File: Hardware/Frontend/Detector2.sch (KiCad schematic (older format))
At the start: 27 parts, among them J4 Conn_Coaxial, U4 OPA145ID, U5 OPA145ID, U6 OPA145ID

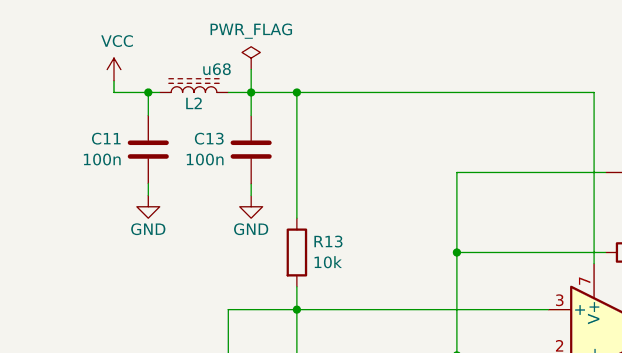
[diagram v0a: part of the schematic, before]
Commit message: add bom
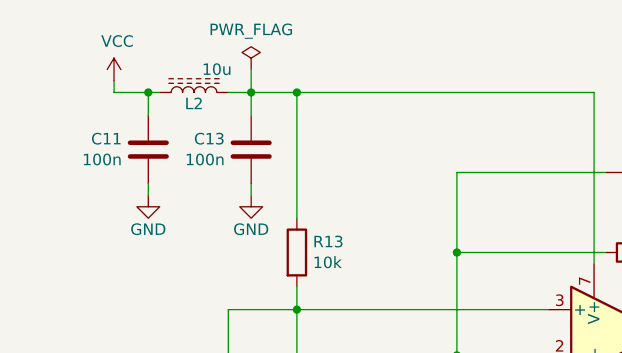
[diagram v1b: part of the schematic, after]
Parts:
- L2: value u68 -> 10u
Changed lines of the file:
@@
 AR Path="/6126C89A/6141383E" Ref="L2"  Part="1"
 F 0 "L2" V 2650 2350 50  0000 C CNN
-F 1 "u68" V 2800 2450 50  0000 C CNN
+F 1 "10u" V 2800 2450 50  0000 C CNN
 F 2 "Inductor_SMD:L_0805_2012Metric" H 2700 2350 50  0001 C CNN
 F 3 "" H 2700 2350 50  0001 C CNN
